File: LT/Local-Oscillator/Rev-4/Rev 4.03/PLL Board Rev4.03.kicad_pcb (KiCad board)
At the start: 2 copper layers, 109.2 x 45.7 mm, 69 parts, among them J1 Conn_01x02_Male, J13 Conn_01x02_Male, J14 Conn_01x02_Male, J15 Conn_01x02_Male, J16 Conn_01x02_Male, J17 Conn_01x02_Male, J18 Conn_Coaxial, J2 Conn_Coaxial, J20 Conn_01x02_Male, J3 Conn_Coaxial, J4 Conn_01x04_Male, J5 Conn_01x02_Male, J7 Conn_01x02_Male, J8 Conn_01x02_Male, Q1 2N5486 JFET, Q2 2N5486 JFET, U1 LMX231X, U2 L7808

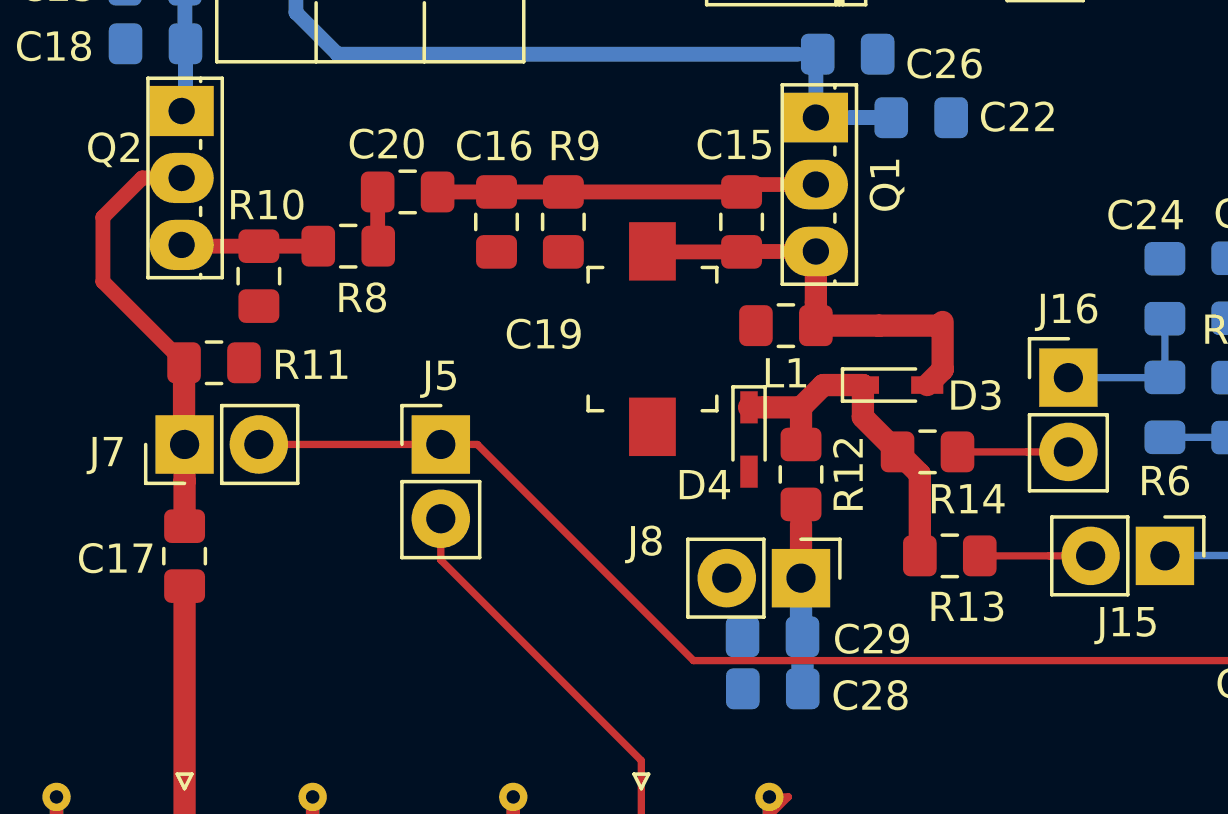
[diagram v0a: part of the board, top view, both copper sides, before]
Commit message: Changed Resistor Symbols
Fixed the resistor symbols from PLL Rev 4.1-4.3
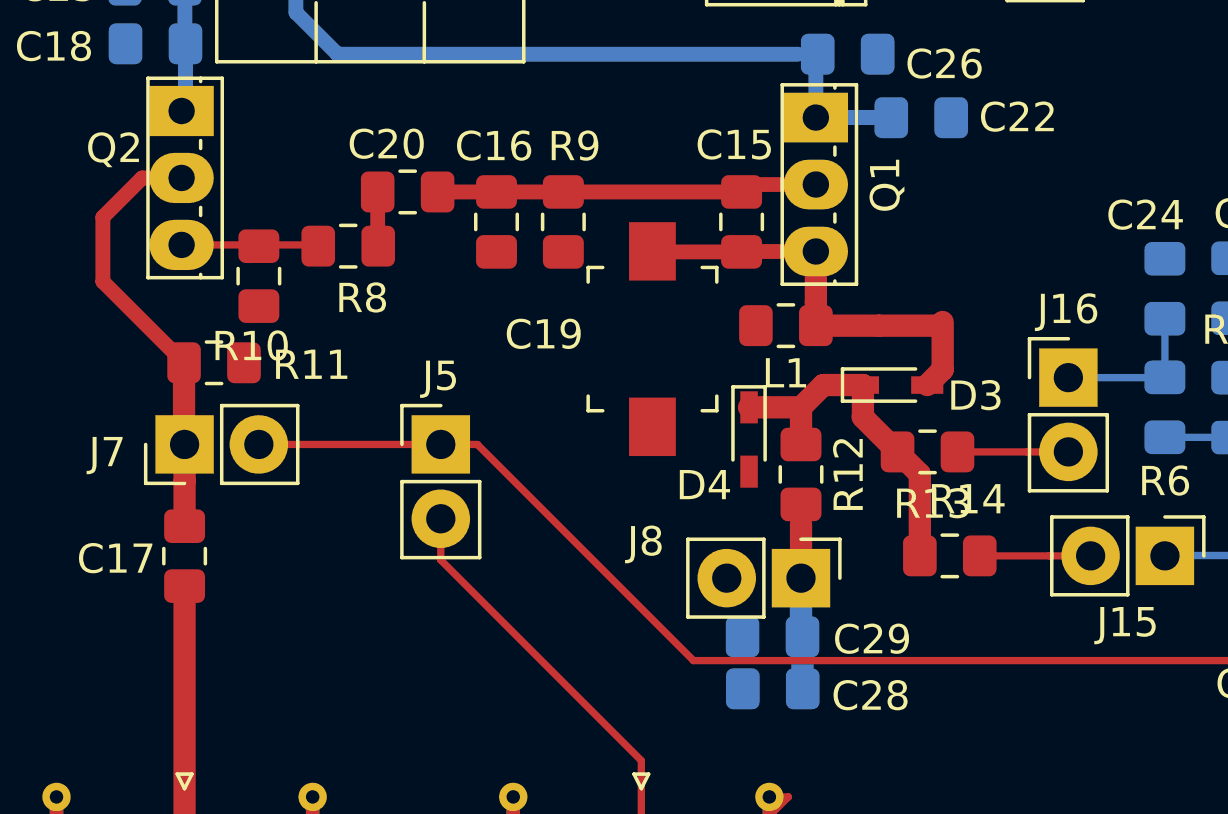
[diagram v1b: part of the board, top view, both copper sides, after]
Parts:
- R13, R14: value 0k -> 0
- turned R10 to 90 degrees
- turned R13 to 180 degrees
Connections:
- R10 pad 1: Net-(Q2-Pad3) -> GND
- R10 pad 2: GND -> Net-(Q2-Pad3)
- R13 pad 1: Net-(D3-Pad1) -> Net-(J15-Pad2)
- R13 pad 2: Net-(J15-Pad2) -> Net-(D3-Pad1)
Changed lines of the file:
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@@
       (effects (font (size 1 1) (thickness 0.15)))
     )
-    (fp_text value 0k (at 0 1.65 180) (layer F.Fab)
+    (fp_text value 0 (at 0 1.65 180) (layer F.Fab)
       (effects (font (size 1 1) (thickness 0.15)))
     )
@@
   )
   (module Resistor_SMD:R_0805_2012Metric_Pad1.15x1.40mm_HandSolder (layer F.Cu)
-    (at 112.785 107.696)
+    (at 112.785 107.696 180)
     (descr "Resistor SMD 0805 (2012 Metric), square (rectangular) end terminal, IPC_7351 nominal with elongated pad for handsoldering. (Body size source: https://docs.google.com/spreadsheets/d/1BsfQQcO9C6DZCsRaXUlFlo91Tg2WpOkGARC1WS5S8t0/edit?usp=sharing), generated with kicad-footprint-generator")
     (tags "resistor handsolder")
@@
       (effects (font (size 1 1) (thickness 0.15)))
     )
-    (fp_text value 0k (at 0 1.65) (layer F.Fab)
+    (fp_text value 0 (at 0 1.65) (layer F.Fab)
       (effects (font (size 1 1) (thickness 0.15)))
     )
@@
       (effects (font (size 0.5 0.5) (thickness 0.08)))
     )
-    (pad 1 smd roundrect (at -1.025 0) (size 1.15 1.4) (layers F.Cu F.Paste F.Mask) (roundrect_rratio 0.217391)
+    (pad 1 smd roundrect (at -1.025 0 180) (size 1.15 1.4) (layers F.Cu F.Paste F.Mask) (roundrect_rratio 0.217391)
+      (net 37 "Net-(J15-Pad2)"))
+    (pad 2 smd roundrect (at 1.025 0 180) (size 1.15 1.4) (layers F.Cu F.Paste F.Mask) (roundrect_rratio 0.217391)
       (net 13 "Net-(D3-Pad1)"))
-    (pad 2 smd roundrect (at 1.025 0) (size 1.15 1.4) (layers F.Cu F.Paste F.Mask) (roundrect_rratio 0.217391)
-      (net 37 "Net-(J15-Pad2)"))
     (model ${KISYS3DMOD}/Resistor_SMD.3dshapes/R_0805_2012Metric.wrl
       (at (xyz 0 0 0))
@@
   )
   (module Resistor_SMD:R_0805_2012Metric_Pad1.15x1.40mm_HandSolder (layer F.Cu)
-    (at 89.154 98.1292 270)
+    (at 89.154 98.1292 90)
     (descr "Resistor SMD 0805 (2012 Metric), square (rectangular) end terminal, IPC_7351 nominal with elongated pad for handsoldering. (Body size source: https://docs.google.com/spreadsheets/d/1BsfQQcO9C6DZCsRaXUlFlo91Tg2WpOkGARC1WS5S8t0/edit?usp=sharing), generated with kicad-footprint-generator")
     (tags "resistor handsolder")
@@
       (effects (font (size 0.5 0.5) (thickness 0.08)))
     )
-    (pad 1 smd roundrect (at -1.025 0 270) (size 1.15 1.4) (layers F.Cu F.Paste F.Mask) (roundrect_rratio 0.217391)
+    (pad 1 smd roundrect (at -1.025 0 90) (size 1.15 1.4) (layers F.Cu F.Paste F.Mask) (roundrect_rratio 0.217391)
+      (net 1 GND))
+    (pad 2 smd roundrect (at 1.025 0 90) (size 1.15 1.4) (layers F.Cu F.Paste F.Mask) (roundrect_rratio 0.217391)
       (net 34 "Net-(Q2-Pad3)"))
-    (pad 2 smd roundrect (at 1.025 0 270) (size 1.15 1.4) (layers F.Cu F.Paste F.Mask) (roundrect_rratio 0.217391)
-      (net 1 GND))
     (model ${KISYS3DMOD}/Resistor_SMD.3dshapes/R_0805_2012Metric.wrl
       (at (xyz 0 0 0))
@@
   (segment (start 141.478 90.424) (end 137.94 90.424) (width 0.25) (layer B.Cu) (net 6) (status 10))
   (segment (start 120.151 103.65) (end 120.142 103.641) (width 0.25) (layer B.Cu) (net 6) (status 30))
-  (segment (start 124.705 103.641) (end 124.714 103.65) (width 0.25) (layer B.Cu) (net 6))
-  (segment (start 120.142 103.641) (end 124.705 103.641) (width 0.25) (layer B.Cu) (net 6))
+  (segment (start 124.705 103.641) (end 124.714 103.65) (width 0.25) (layer B.Cu) (net 6) (status 30))
+  (segment (start 120.142 103.641) (end 124.705 103.641) (width 0.25) (layer B.Cu) (net 6) (status 30))
   (segment (start 105.918 94.996) (end 105.664 95.25) (width 0.508) (layer F.Cu) (net 7) (status 30))
   (segment (start 108.204 94.996) (end 105.918 94.996) (width 0.508) (layer F.Cu) (net 7) (status 30))
@@
   (segment (start 184.8358 87.9856) (end 184.8358 93.6498) (width 0.762) (layer F.Cu) (net 12) (status 30))
   (segment (start 111.76 104.902) (end 110.998 104.14) (width 0.762) (layer F.Cu) (net 13) (status 20))
-  (segment (start 111.76 107.696) (end 111.76 104.902) (width 0.762) (layer F.Cu) (net 13) (status 10))
   (segment (start 110.064 101.854) (end 109.814 101.854) (width 0.25) (layer F.Cu) (net 13) (status 30))
   (segment (start 105.918 102.366) (end 105.918 102.616) (width 0.25) (layer F.Cu) (net 13) (status 30))
@@
   (segment (start 109.814 102.9364) (end 109.814 101.854) (width 0.762) (layer F.Cu) (net 13) (status 20))
   (segment (start 109.8042 102.9462) (end 109.814 102.9364) (width 0.25) (layer F.Cu) (net 13))
+  (segment (start 111.76 107.696) (end 111.76 104.902) (width 0.762) (layer F.Cu) (net 13))
   (segment (start 114.663787 87.376) (end 112.268 87.376) (width 0.508) (layer B.Cu) (net 14) (status 20))
   (segment (start 116.078 87.376) (end 114.663787 87.376) (width 0.508) (layer B.Cu) (net 14) (status 10))
@@
   (segment (start 86.614 103.886) (end 86.614 105.136) (width 0.762) (layer F.Cu) (net 33) (status 10))
   (segment (start 86.5298 97.0788) (end 86.5124 97.0614) (width 0.25) (layer F.Cu) (net 34) (status 30))
-  (segment (start 91.186 97.1042) (end 89.154 97.1042) (width 0.508) (layer F.Cu) (net 34) (status 30))
   (segment (start 86.5552 97.1042) (end 86.5124 97.0614) (width 0.25) (layer F.Cu) (net 34) (status 30))
-  (segment (start 89.154 97.1042) (end 86.5552 97.1042) (width 0.508) (layer F.Cu) (net 34) (status 30))
-  (segment (start 122.428 99.568) (end 122.428 101.6) (width 0.25) (layer B.Cu) (net 35))
+  (segment (start 91.1432 97.0614) (end 91.186 97.1042) (width 0.25) (layer F.Cu) (net 34))
+  (segment (start 86.5124 97.0614) (end 91.1432 97.0614) (width 0.25) (layer F.Cu) (net 34))
+  (segment (start 122.428 99.568) (end 122.428 101.6) (width 0.25) (layer B.Cu) (net 35) (status 30))
   (segment (start 120.142 101.591) (end 120.142 99.586) (width 0.25) (layer B.Cu) (net 36) (status 30))
   (segment (start 120.133 101.6) (end 120.142 101.591) (width 0.25) (layer B.Cu) (net 36) (status 30))
   (segment (start 116.84 101.6) (end 120.133 101.6) (width 0.25) (layer B.Cu) (net 36) (status 30))
-  (segment (start 116.187787 107.696) (end 113.81 107.696) (width 0.25) (layer F.Cu) (net 37) (status 20))
   (segment (start 117.602 107.696) (end 116.187787 107.696) (width 0.25) (layer F.Cu) (net 37) (status 10))
+  (segment (start 113.81 107.696) (end 116.187787 107.696) (width 0.25) (layer F.Cu) (net 37))
   (segment (start 115.425787 104.14) (end 113.048 104.14) (width 0.25) (layer F.Cu) (net 38) (status 20))
   (segment (start 116.84 104.14) (end 115.425787 104.14) (width 0.25) (layer F.Cu) (net 38) (status 10))
